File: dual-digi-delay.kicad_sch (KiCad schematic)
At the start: 46 parts, among them J10 Delay Audio, J11 Delay2 Source, J12 Input Audio, J13 Delay1_CV, J14 Delay2_CV, J15 MidBoardPowerSend, J16 Delay Send, J17 Delay Return, J18 Delay Time Control, J19 LowerBoardPowerSend, J20 Main Power, J21 Delay Return, J22 Delay Send, J23 Delay Time Control, J24 MidBoardPowerRecv, J25 Delay Out, J26 Delay Audio, J27 Delay2_CV, J28 Output Audio, J29 Delay2 Source, J30 TopBoardPowerRecv, J31 Feedback Audio, J32 Input Audio, J33 Delay1_CV, J7 Output Audio, J8 Delay Out, J9 Feedback Audio

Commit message: Changes after tweaking
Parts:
- removed J16: Delay Send, Connector_PinSocket_2.54mm:PinSocket_1x02_P2.54mm_Vertical, symbol Connector:Conn_01x02_Female
- removed J17: Delay Return, Connector_PinSocket_2.54mm:PinSocket_1x02_P2.54mm_Vertical, symbol Connector:Conn_01x02_Female
- removed J21: Delay Return, Connector_PinHeader_2.54mm:PinHeader_1x02_P2.54mm_Vertical, symbol Connector:Conn_01x02_Male
- removed J22: Delay Send, Connector_PinHeader_2.54mm:PinHeader_1x02_P2.54mm_Vertical, symbol Connector:Conn_01x02_Male
- added J16: Delay Send/Recv, Connector_PinHeader_2.54mm:PinHeader_1x04_P2.54mm_Vertical, symbol Connector:Conn_01x04_Male
- added J17: Delay Send/Recv, Connector_PinSocket_2.54mm:PinSocket_1x04_P2.54mm_Vertical, symbol Connector:Conn_01x04_Female
- H11, H12, H13, H14, H15, H16, H19, H3, H4, H5, H6, H7, H8: now left out of the parts list
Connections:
- net DelayBuffers/DELAY1_OUT: now also J17.4 (Pin_4)
- net DelayBuffers/DELAY2_OUT: now also J17.3 (Pin_3)
- net DelayOut/DELAY1_WET: now also J16.4 (Pin_4)
- net DelayOut/DELAY2_WET: now also J16.3 (Pin_3)
- net InputMix/INPUT_MIX: now also J16.1 (Pin_1)
- net PT2399-Delay-1/AUDIO_IN: now also J17.1 (Pin_1)
- net PT2399-Delay-2/AUDIO_IN: now also J17.2 (Pin_2)
- net at J11.2 (Pin_2): now also J16.2 (Pin_2)
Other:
- moved on the sheet: J18

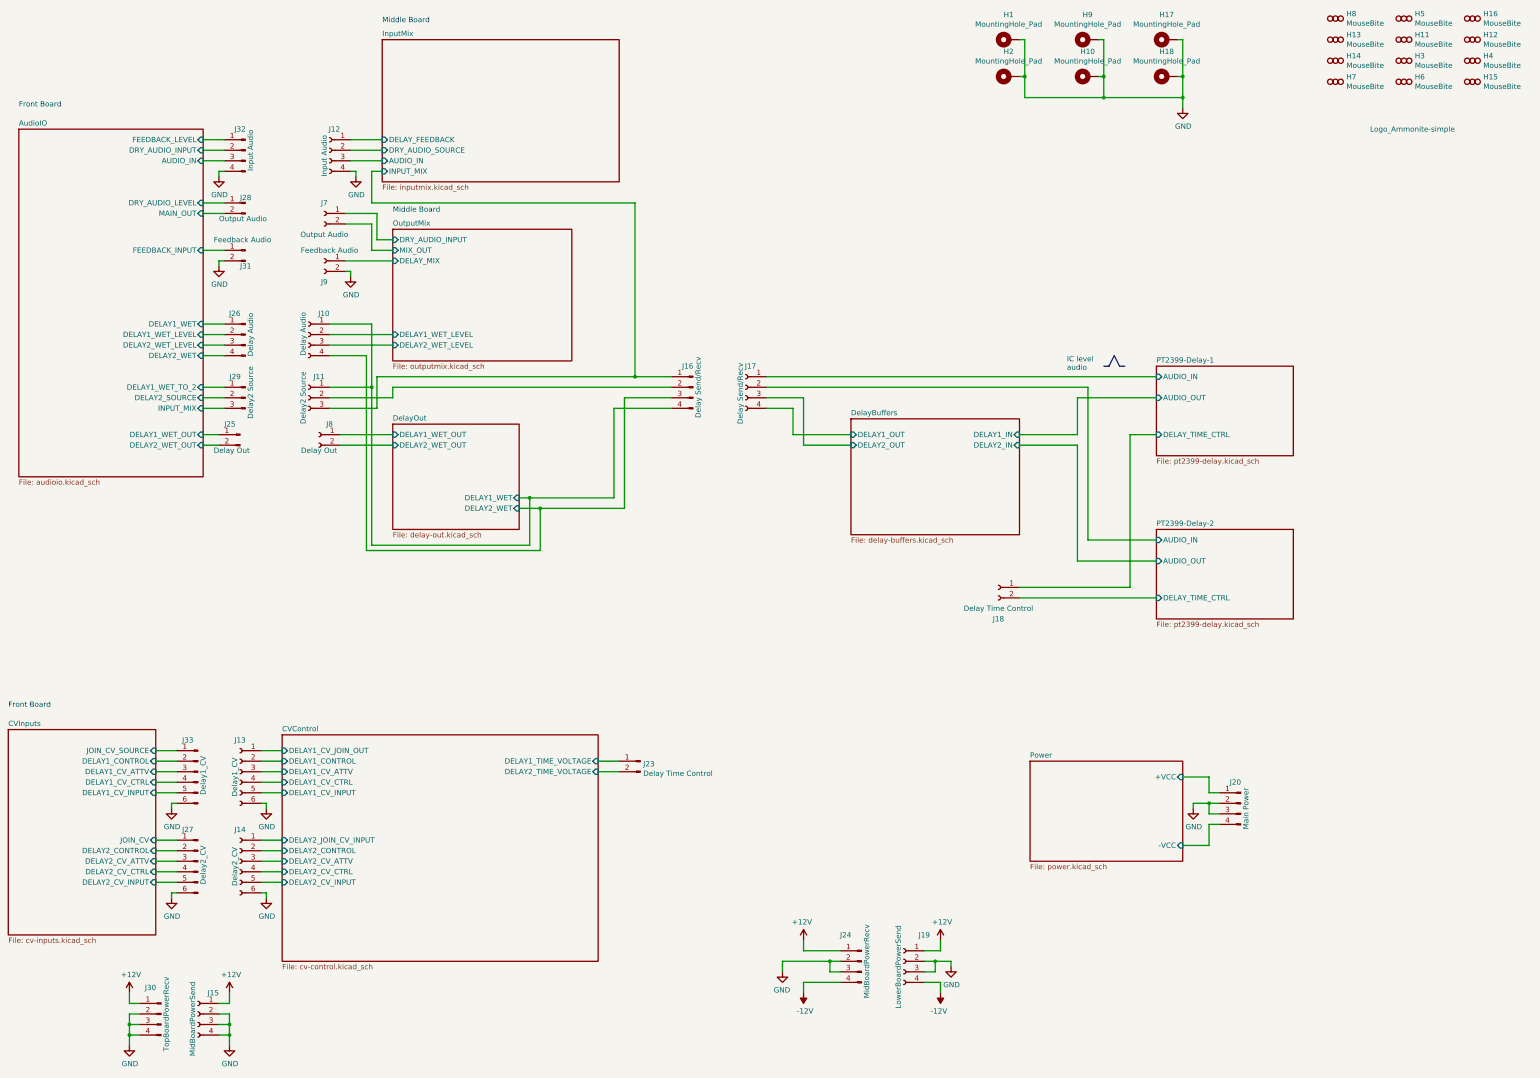
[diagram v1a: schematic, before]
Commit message: Tweaks and fixes for rev 4
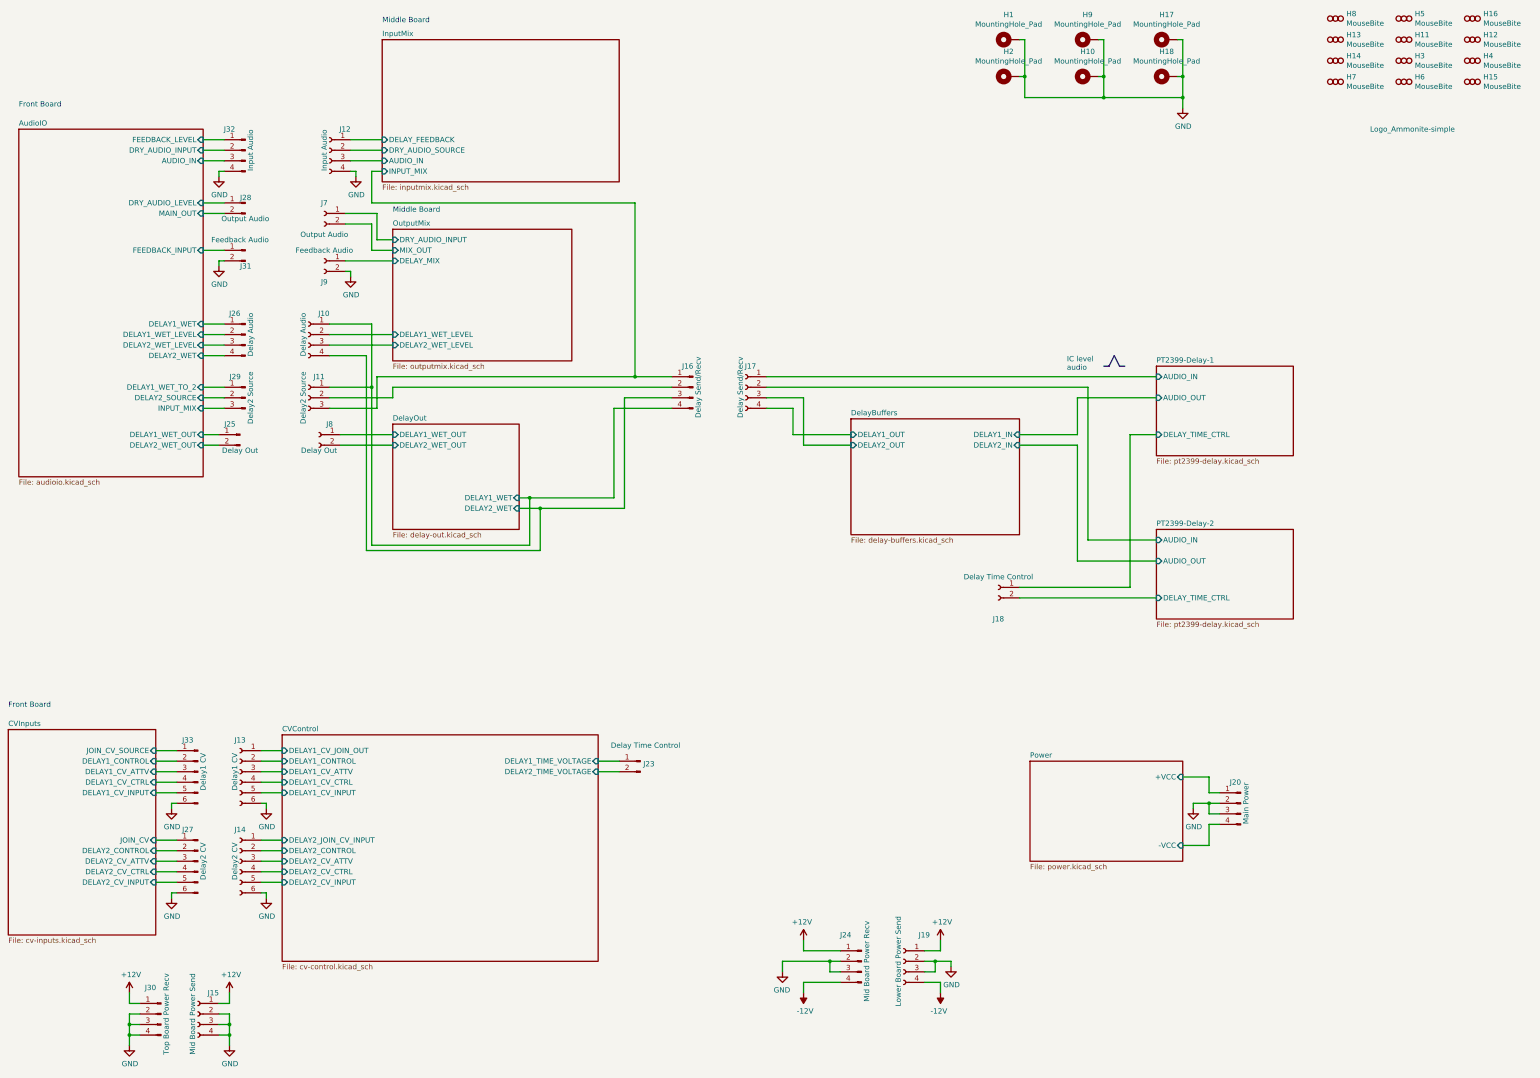
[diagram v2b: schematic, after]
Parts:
- J10: value Delay Audio -> Conn_1x04_Skt; Note (none) -> Delay Audio
- J11: value Delay2 Source -> Conn_1x03_Skt; Note (none) -> Delay2 Source
- J12: value Input Audio -> Conn_1x04_Skt; Note (none) -> Input Audio
- J13: value Delay1_CV -> Conn_1x06_Skt; Note (none) -> Delay1 CV
- J14: value Delay2_CV -> Conn_1x06_Skt; Note (none) -> Delay2 CV
- J15: value MidBoardPowerSend -> Conn_1x04_Skt; Note (none) -> Mid Board Power Send
- J16: value Delay Send/Recv -> Conn_1x04_Pin; Note (none) -> Delay Send/Recv
- J17: value Delay Send/Recv -> Conn_1x04_Skt; Note (none) -> Delay Send/Recv
- J18: value Delay Time Control -> Conn_1x04_Skt; Note (none) -> Delay Time Control
- J19: value LowerBoardPowerSend -> Conn_1x04_Skt; Note (none) -> Lower Board Power Send
- J20: value Main Power -> Molex_1x04_KK-254; Note (none) -> Main Power
- J23: value Delay Time Control -> Conn_1x02_Pin; Note (none) -> Delay Time Control
- J24: value MidBoardPowerRecv -> Conn_1x04_Pin; Note (none) -> Mid Board Power Recv
- J25: value Delay Out -> Conn_1x02_Pin; Note (none) -> Delay Out
- J26: value Delay Audio -> Conn_1x04_Pin; Note (none) -> Delay Audio
- J27: value Delay2_CV -> Conn_1x06_Pin; Note (none) -> Delay2 CV
- J28: value Output Audio -> Conn_1x02_Pin; Note (none) -> Output Audio
- J29: value Delay2 Source -> Conn_1x03_Pin; Note (none) -> Delay2 Source
- J30: value TopBoardPowerRecv -> Conn_1x04_Pin; Note (none) -> Top Board Power Recv
- J31: value Feedback Audio -> Conn_1x02_Pin; Note (none) -> Feedback Audio
- J32: value Input Audio -> Conn_1x04_Pin; Note (none) -> Input Audio
- J33: value Delay1_CV -> Conn_1x06_Pin; Note (none) -> Delay1 CV
- J7: value Output Audio -> Conn_1x02_Skt; Note (none) -> Output Audio
- J8: value Delay Out -> Conn_1x02_Skt; Note (none) -> Delay Out
- J9: value Feedback Audio -> Conn_1x02_Skt; Note (none) -> Feedback Audio
